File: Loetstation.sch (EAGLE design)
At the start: 69 parts, among them IC1 ATMEGA328PB-AU, IC2 LM75AD,112, IC3 CD4050BD, IC4 7805DT, IC5 AMS1117-3.3V, IC6 TL082D, J1 22-27-2021-02, J2 AVR_SPI_PROG_3X2TESTPOINTS, J3 22-27-2041-04, J4 22-27-2041-04, T1 SI7489DP-T1-E3, T2 SI7489DP-T1-E3, T3 BC847, T4 BC847, X1 CSTCE16M0V53-R0, X2 ENCODER-SWITCH, X3 DISPLAY_TFT_1,8, X4 22-27-2051-05

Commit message: changed capacitor package from 0402 to 0603
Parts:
- C1, C10, C11, C12, C13, C14, C3, C6, C7, C9: device resistor:C-EUC0402 -> resistor:C-EUC0603
- R18, R19: device resistor:R-EU_R0603 -> resistor:R-EU_R0402

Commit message: Power-MOSFETs durch FDS9435A getauscht
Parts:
- removed T1, T2: SI7489DP-T1-E3, SamacSys_Parts:SI7489DP-T1-E3
- added IC7, IC8: FDS9435A, SamacSys_Parts:FDS9435A
- D1: value (none) -> 1N4148WS
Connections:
- net KOLBEN1: now also IC7.D_1, IC7.D_2, IC7.D_3, IC7.D_4; no longer T2.DRAIN@1, T2.DRAIN@2, T2.DRAIN@3, T2.DRAIN@4, T2.DRAIN@5
- net KOLBEN2: now also IC8.D_1, IC8.D_2, IC8.D_3, IC8.D_4; no longer T1.DRAIN@1, T1.DRAIN@2, T1.DRAIN@3, T1.DRAIN@4, T1.DRAIN@5
- net N$4: now also IC8.G; no longer T1.GATE
- net N$5: now also IC7.G; no longer T2.GATE
- net V_IN: now also IC7.S_1, IC7.S_2, IC7.S_3, IC8.S_1, IC8.S_2, IC8.S_3; no longer T1.SOURCE@1, T1.SOURCE@2, T1.SOURCE@3, T2.SOURCE@1, T2.SOURCE@2, T2.SOURCE@3
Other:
- moved on the sheet: C10, C11, C12, C13, C14, C4, C5, C7, C9, D2, D3, IC4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

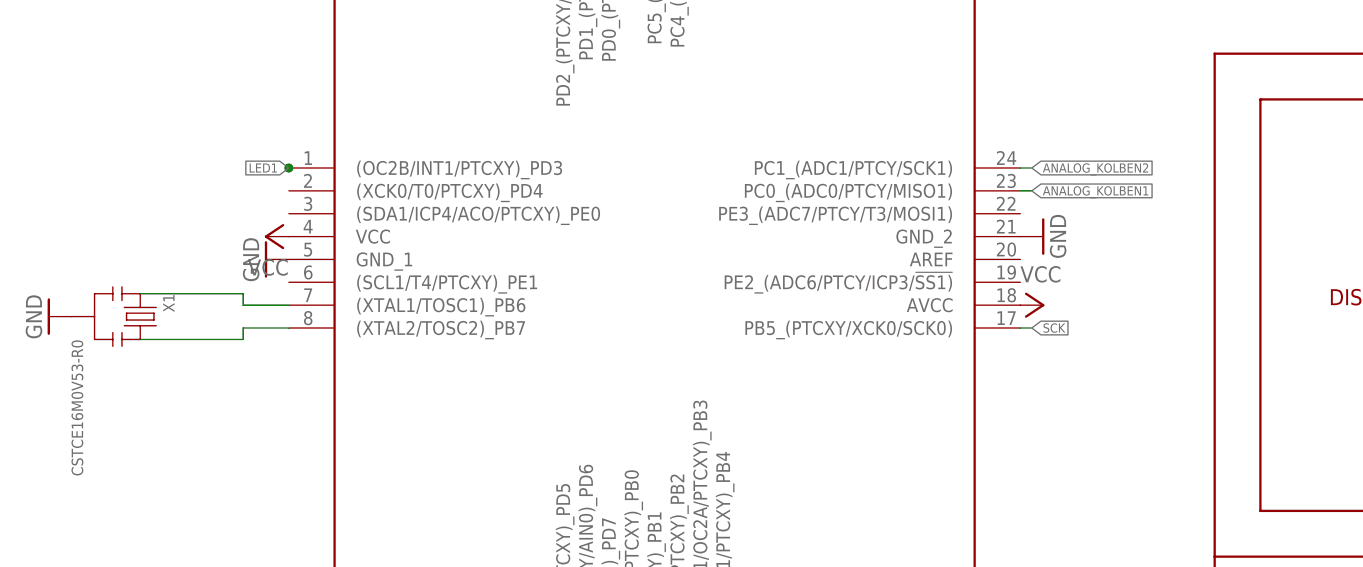
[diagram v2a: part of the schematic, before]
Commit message: Abblock Kondensatoren für µC hinzugefügt
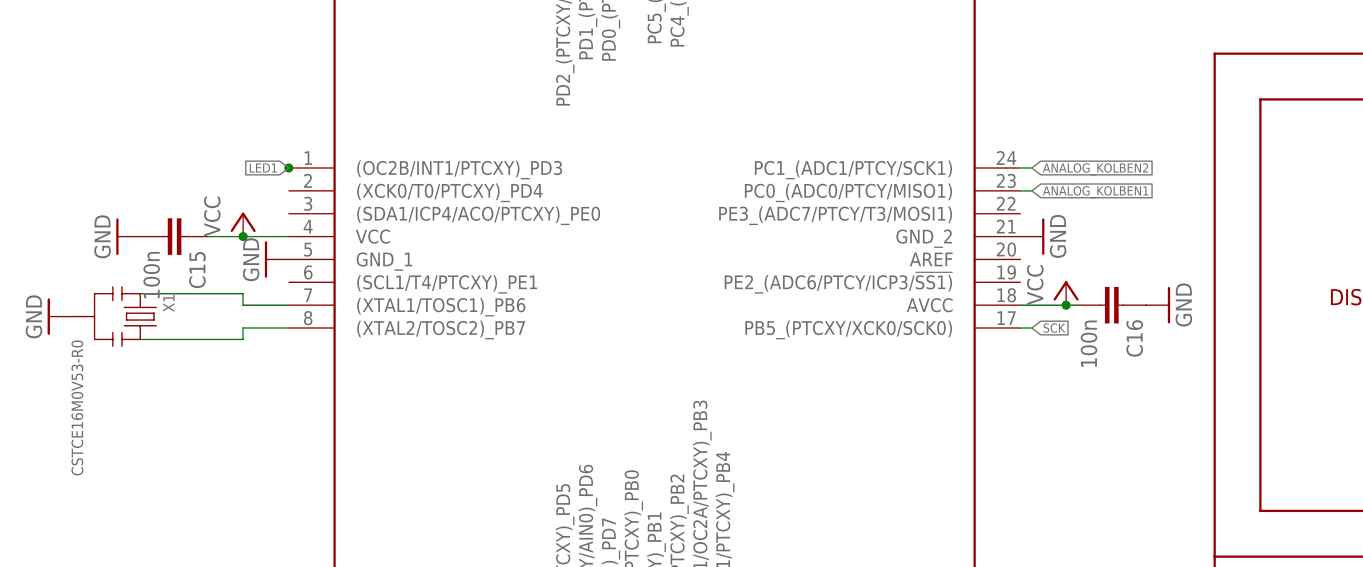
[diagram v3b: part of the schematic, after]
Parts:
- added C15, C16: 100n, resistor:C-EUC0603
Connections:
- net GND: now also C15.2, C16.1
- net VCC: now also C15.1, C16.2
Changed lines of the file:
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@@
 <?xml version="1.0" encoding="utf-8"?>
 <!DOCTYPE eagle SYSTEM "eagle.dtd">
-<eagle version="9.2.1">
+<eagle version="9.2.2">
 <drawing>
 <settings>
@@
 <setting verticaltext="up"/>
 </settings>
-<grid distance="0.1" unitdist="inch" unit="inch" style="lines" multiple="1" display="no" altdistance="0.01" altunitdist="inch" altunit="inch"/>
+<grid distance="50" unitdist="mil" unit="mil" style="lines" multiple="1" display="no" altdistance="0.01" altunitdist="inch" altunit="inch"/>
 <layers>
 <layer number="1" name="Top" color="4" fill="1" visible="no" active="no"/>
@@
 <part name="IC7" library="SamacSys_Parts" deviceset="FDS9435A" device=""/>
 <part name="IC8" library="SamacSys_Parts" deviceset="FDS9435A" device=""/>
+<part name="C15" library="resistor" library_urn="urn:adsk.eagle:library:348" deviceset="C-EU" device="C0603" package3d_urn="urn:adsk.eagle:package:23616/2" value="100n"/>
+<part name="GND37" library="supply1" library_urn="urn:adsk.eagle:library:371" deviceset="GND" device=""/>
+<part name="C16" library="resistor" library_urn="urn:adsk.eagle:library:348" deviceset="C-EU" device="C0603" package3d_urn="urn:adsk.eagle:package:23616/2" value="100n"/>
+<part name="GND38" library="supply1" library_urn="urn:adsk.eagle:library:371" deviceset="GND" device=""/>
 </parts>
 <sheets>
@@
 <attribute name="VALUE" x="57.15" y="53.34" size="1.778" layer="96" rot="MR0"/>
 </instance>
-<instance part="P+1" gate="VCC" x="-123.19" y="107.95" smashed="yes" rot="R90">
-<attribute name="VALUE" x="-120.65" y="105.41" size="1.778" layer="96" rot="R180"/>
+<instance part="P+1" gate="VCC" x="-125.73" y="110.49" smashed="yes">
+<attribute name="VALUE" x="-128.27" y="107.95" size="1.778" layer="96" rot="R90"/>
 </instance>
 <instance part="P+8" gate="VCC" x="60.96" y="49.53" smashed="yes" rot="R270">
@@
 <attribute name="VALUE" x="-34.29" y="110.49" size="1.778" layer="96" rot="MR270"/>
 </instance>
-<instance part="P+6" gate="VCC" x="-36.83" y="100.33" smashed="yes" rot="R270">
-<attribute name="VALUE" x="-39.37" y="102.87" size="1.778" layer="96"/>
+<instance part="P+6" gate="VCC" x="-34.29" y="102.87" smashed="yes">
+<attribute name="VALUE" x="-36.83" y="100.33" size="1.778" layer="96" rot="R90"/>
 </instance>
 <instance part="IC6" gate="B" x="91.44" y="133.35" smashed="yes">
@@
 <attribute name="NAME" x="214.63" y="121.92" size="1.778" layer="95" align="center-left"/>
 <attribute name="VALUE" x="214.63" y="119.38" size="1.778" layer="96" align="center-left"/>
+</instance>
+<instance part="C15" gate="G$1" x="-132.08" y="107.95" smashed="yes" rot="R270">
+<attribute name="NAME" x="-131.699" y="106.426" size="1.778" layer="95" rot="R270"/>
+<attribute name="VALUE" x="-136.779" y="106.426" size="1.778" layer="96" rot="R270"/>
+</instance>
+<instance part="GND37" gate="1" x="-139.7" y="107.95" smashed="yes" rot="MR90">
+<attribute name="VALUE" x="-142.24" y="105.41" size="1.778" layer="96" rot="MR90"/>
+</instance>
+<instance part="C16" gate="G$1" x="-27.94" y="100.33" smashed="yes" rot="R270">
+<attribute name="NAME" x="-27.559" y="98.806" size="1.778" layer="95" rot="R270"/>
+<attribute name="VALUE" x="-32.639" y="98.806" size="1.778" layer="96" rot="R270"/>
+</instance>
+<instance part="GND38" gate="1" x="-22.86" y="100.33" smashed="yes" rot="MR270">
+<attribute name="VALUE" x="-20.32" y="102.87" size="1.778" layer="96" rot="MR270"/>
 </instance>
 </instances>
@@
 <pinref part="IC1" gate="G$1" pin="VCC"/>
 <pinref part="P+1" gate="VCC" pin="VCC"/>
+<wire x1="-125.73" y1="107.95" x2="-120.65" y2="107.95" width="0.1524" layer="91"/>
+<pinref part="C15" gate="G$1" pin="1"/>
+<wire x1="-129.54" y1="107.95" x2="-125.73" y2="107.95" width="0.1524" layer="91"/>
+<junction x="-125.73" y="107.95"/>
 </segment>
 <segment>
@@
 <pinref part="IC1" gate="G$1" pin="AVCC"/>
 <pinref part="P+6" gate="VCC" pin="VCC"/>
+<wire x1="-34.29" y1="100.33" x2="-39.37" y2="100.33" width="0.1524" layer="91"/>
+<pinref part="C16" gate="G$1" pin="2"/>
+<wire x1="-33.02" y1="100.33" x2="-34.29" y2="100.33" width="0.1524" layer="91"/>
+<junction x="-34.29" y="100.33"/>
 </segment>
 <segment>
@@
 <pinref part="GND6" gate="1" pin="GND"/>
 </segment>
+<segment>
+<pinref part="C15" gate="G$1" pin="2"/>
+<pinref part="GND37" gate="1" pin="GND"/>
+</segment>
+<segment>
+<pinref part="C16" gate="G$1" pin="1"/>
+<pinref part="GND38" gate="1" pin="GND"/>
+</segment>
 </net>
